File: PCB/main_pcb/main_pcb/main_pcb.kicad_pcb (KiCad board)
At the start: 2 copper layers, 163.5 x 133.5 mm, 55 parts, among them J1 Conn_01x20_Socket, J2 Conn_01x20_Socket, J3 Conn_01x09_Socket, SW0_Header1 B6B-XH-A, SW1_Header1 B6B-XH-A

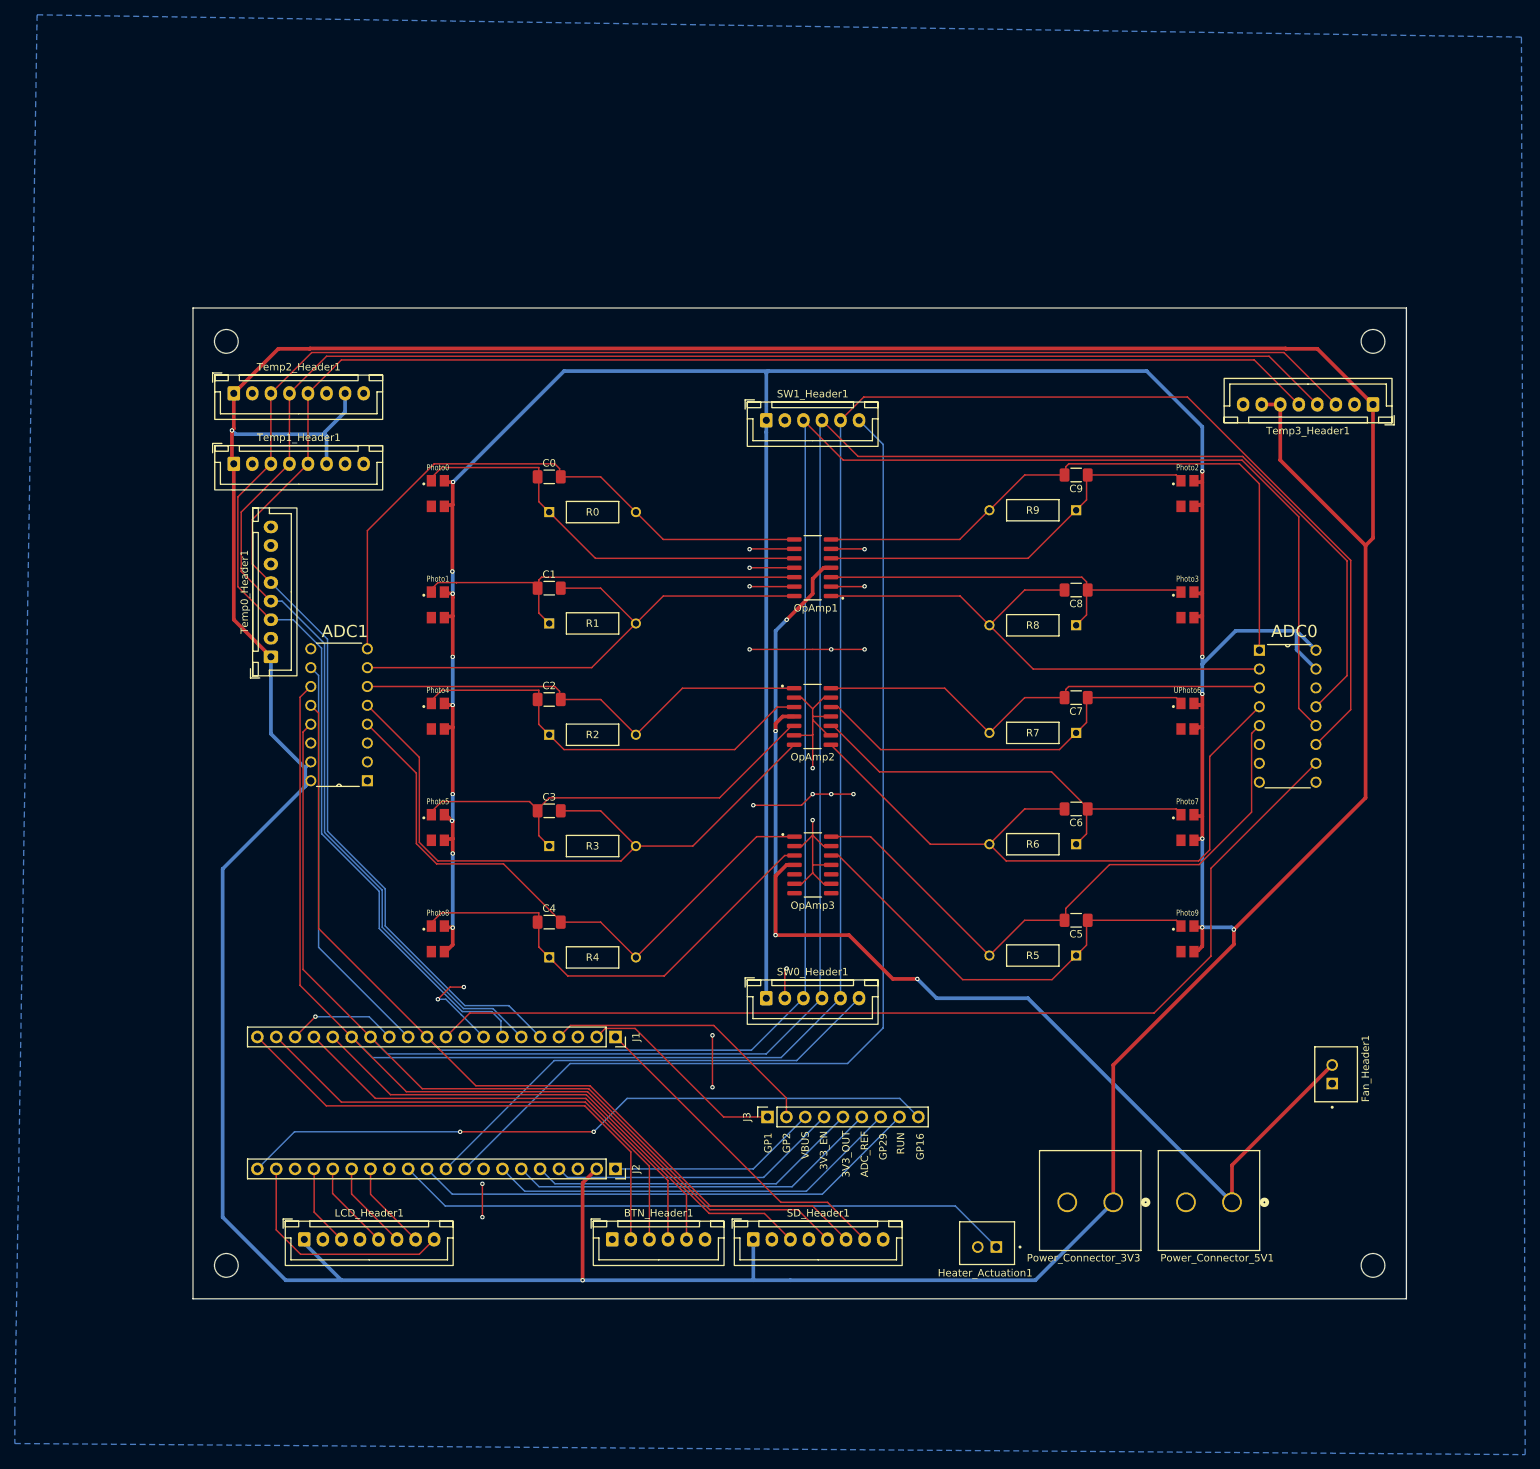
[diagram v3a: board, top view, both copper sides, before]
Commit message: Fully seperated analog ground from digital ground on the main PCB.
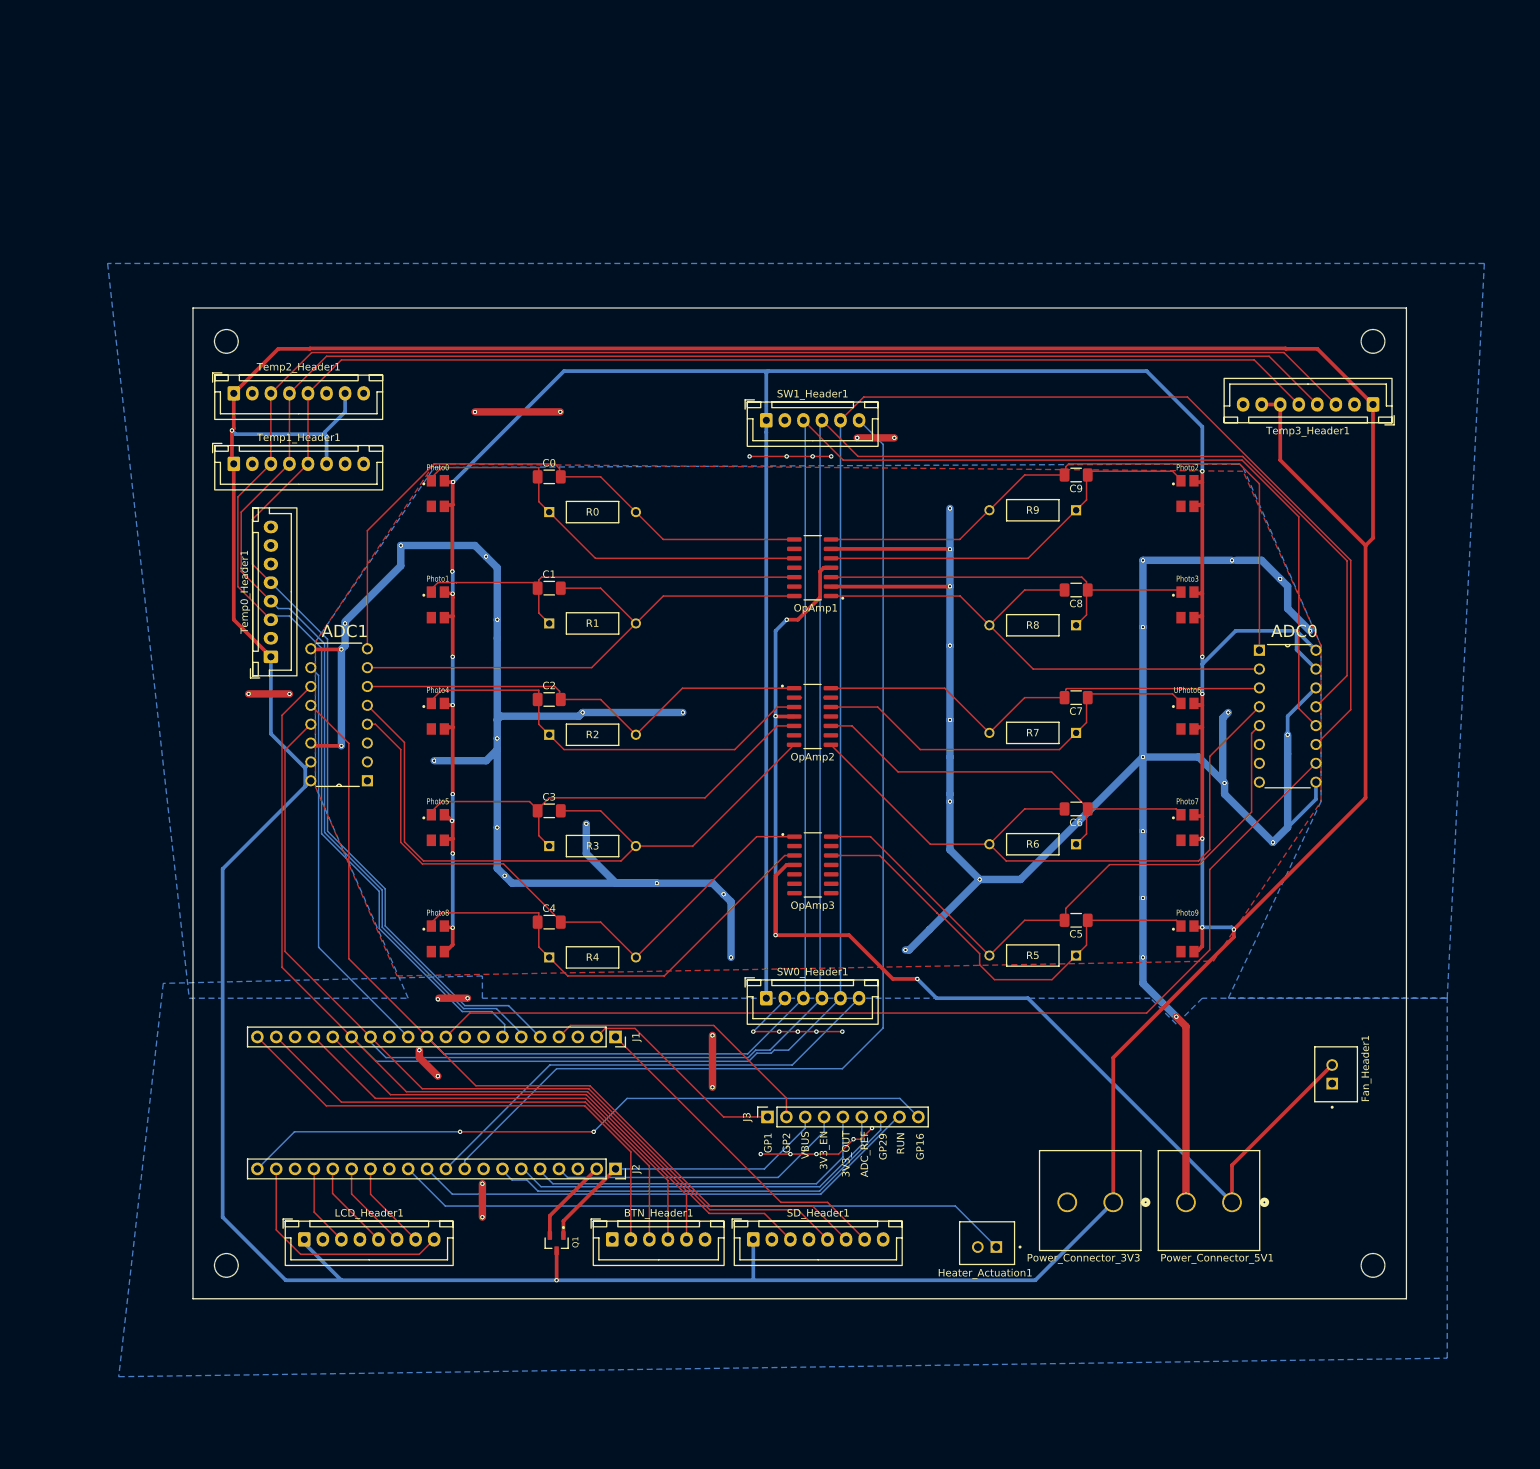
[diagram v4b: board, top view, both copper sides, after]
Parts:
- added Q1: DMG2305UX-7, DMG2305UX_7:SOT91P240X110-3N_DMG2305UX-7, F.Cu at (66.5, 163.5)
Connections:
- J2 pad 2: +3.3V -> VSYS
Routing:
- net GND: track 144.3 -> 581.7 mm, vias 22 -> 66
- net VBUS: track 28.5 -> 41.2 mm
- net +3.3V: track 994.7 -> 982.8 mm
- net VSYS: track 0.00 -> 11.6 mm
- net 3V3_OUT: track 45.4 -> 48.7 mm
- net SPI1_SCK: track 362.2 -> 365.0 mm
- net SPI1_MOSI: track 375.2 -> 377.7 mm
- net ADC_VREF: track 50.8 -> 53.0 mm
- net OpOut8: track 83.0 -> 84.8 mm
- net GPIO29: track 56.3 -> 57.5 mm
- net 3V3_EN: track 39.6 -> 40.7 mm
- net OpOut5: track 91.6 -> 92.8 mm
- net OpIn9: track 60.0 -> 60.9 mm
- net I2C0_SCL: track 256.2 -> 256.9 mm
- net OpIn2: track 54.5 -> 55.2 mm
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- added copper zone on F.Cu, net GND

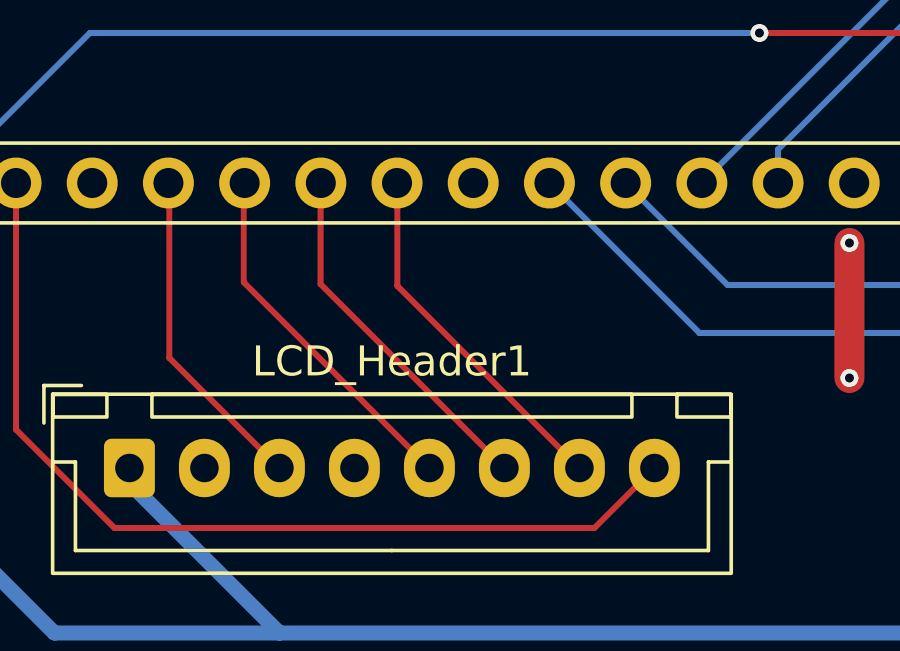
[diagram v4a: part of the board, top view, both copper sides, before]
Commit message: Switched around regsel and reset pins for display header on main PCB.
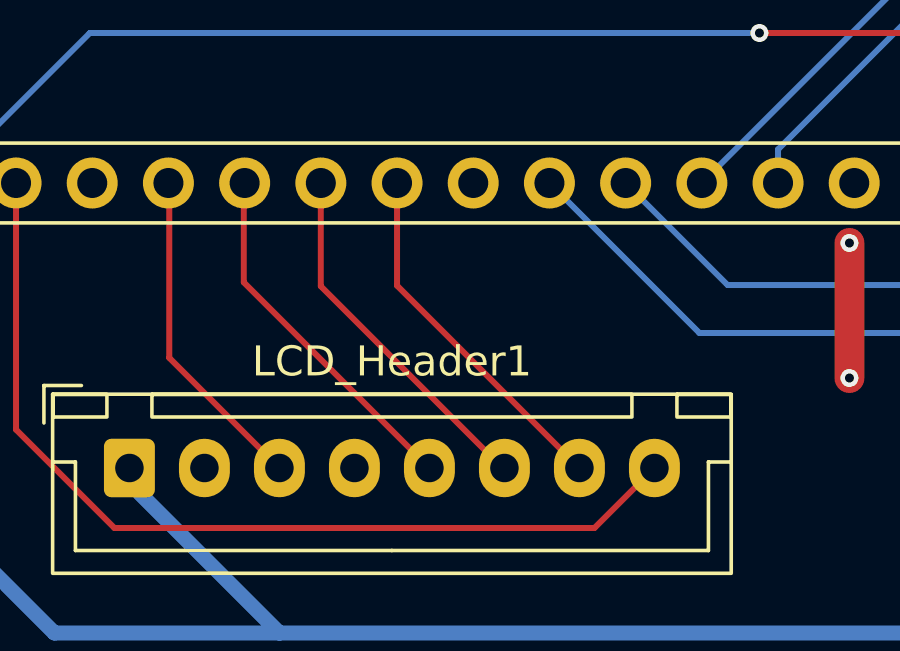
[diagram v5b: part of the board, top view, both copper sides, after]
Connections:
- J2 pad 14: DISP_RST -> DISP REGSEL
- J2 pad 15: DISP REGSEL -> DISP_RST
- LCD_Header1 pad 6: DISP REGSEL -> DISP_RST
- LCD_Header1 pad 7: DISP_RST -> DISP REGSEL
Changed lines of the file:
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@@
 			(layers "*.Cu" "*.Mask")
 			(remove_unused_layers no)
-			(net 47 "DISP_RST")
+			(net 43 "DISP REGSEL")
 			(pinfunction "Pin_14")
 			(pintype "passive")
@@
 			(layers "*.Cu" "*.Mask")
 			(remove_unused_layers no)
-			(net 43 "DISP REGSEL")
+			(net 47 "DISP_RST")
 			(pinfunction "Pin_15")
 			(pintype "passive")
@@
 			(layer "F.Fab")
 		)
+		(fp_text user "${REFERENCE}"
+			(at -2 7.5 0)
+			(unlocked yes)
+			(layer "F.Fab")
+			(effects
+				(font
+					(size 1 1)
+					(thickness 0.15)
+				)
+			)
+		)
 		(pad "1" thru_hole circle
 			(at 0 0)
@@
 			(layers "*.Cu" "*.Mask")
 			(remove_unused_layers no)
-			(net 43 "DISP REGSEL")
+			(net 47 "DISP_RST")
 			(pinfunction "6")
 			(pintype "passive")
@@
 			(layers "*.Cu" "*.Mask")
 			(remove_unused_layers no)
-			(net 47 "DISP_RST")
+			(net 43 "DISP REGSEL")
 			(pinfunction "7")
 			(pintype "passive")
@@
 			(layer "F.Fab")
 		)
+		(fp_text user "${REFERENCE}"
+			(at -4 7.5 0)
+			(unlocked yes)
+			(layer "F.Fab")
+			(effects
+				(font
+					(size 1 1)
+					(thickness 0.15)
+				)
+			)
+		)
 		(pad "1" thru_hole circle
 			(at 0 0)
@@
 	)
 	(segment
-		(start 38.871067 156.871067)
-		(end 38.871067 153.508933)
+		(start 41.42 153.5)
+		(end 41.42 156.92)
 		(width 0.2)
 		(layer "F.Cu")
@@
 	)
 	(segment
-		(start 45 163)
-		(end 38.871067 156.871067)
+		(start 41.42 156.92)
+		(end 47.5 163)
 		(width 0.2)
 		(layer "F.Cu")
@@
 	)
 	(segment
-		(start 38.871067 153.508933)
-		(end 38.88 153.5)
+		(start 41.429981 153.509981)
+		(end 41.42 153.5)
 		(width 0.2)
 		(layer "F.Cu")
@@
 	)
 	(segment
-		(start 47.5 163)
-		(end 41.429981 156.929981)
+		(start 44.94 163)
+		(end 38.88 156.94)
 		(width 0.2)
 		(layer "F.Cu")
@@
 	)
 	(segment
-		(start 41.429981 153.509981)
-		(end 41.42 153.5)
+		(start 38.88 156.94)
+		(end 38.88 153.5)
 		(width 0.2)
 		(layer "F.Cu")
@@
 	)
 	(segment
-		(start 41.429981 156.929981)
-		(end 41.429981 153.509981)
+		(start 45 163)
+		(end 44.94 163)
+		(width 0.2)
+		(layer "F.Cu")
+		(net 47)
+	)
+	(segment
+		(start 38.871067 153.508933)
+		(end 38.88 153.5)
 		(width 0.2)
 		(layer "F.Cu")
@@
 	)
 	(segment
-		(start 33.828501 153.528501)
-		(end 33.8 153.5)
+		(start 37.5 163)
+		(end 33.828501 159.328501)
 		(width 0.2)
 		(layer "F.Cu")
@@
 	)
 	(segment
-		(start 37.5 163)
-		(end 33.828501 159.328501)
+		(start 33.828501 153.528501)
+		(end 33.8 153.5)
 		(width 0.2)
 		(layer "F.Cu")
@@
 			(pts
 				(xy 158.5 58.5) (xy 159 59) (xy 169.5 83) (xy 169.5 104) (xy 157 130.5) (xy 186.5 130.5) (xy 191.5 31.5)
-				(xy 6 31.5) (xy 17 130.5) (xy 46.5 130.5) (xy 34 102) (xy 34 82.5) (xy 50 59) (xy 158 58.5) (xy 158 58.5)
+				(xy 6 31.5) (xy 17 130.5) (xy 46.5 130.5) (xy 34 102) (xy 34 82.5) (xy 50 59) (xy 158 58.5)
 			)
 		)

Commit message: A lot of changes, display logic and some error handling
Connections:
- net DISP REGSEL renamed DISP RST
- net DISP_RST renamed DISP_A0
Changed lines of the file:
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@@
 	(net 41 "ADC_VREF")
 	(net 42 "3V3_OUT")
-	(net 43 "DISP REGSEL")
+	(net 43 "DISP RST")
 	(net 44 "+3.3V")
 	(net 45 "HEATER_ON")
 	(net 46 "SPI1_CSn_TD1")
-	(net 47 "DISP_RST")
+	(net 47 "DISP_A0")
 	(net 48 "SPI1_MOSI")
 	(net 49 "SPI0_SCK")
@@
 			(layers "*.Cu" "*.Mask")
 			(remove_unused_layers no)
-			(net 43 "DISP REGSEL")
+			(net 43 "DISP RST")
 			(pinfunction "Pin_14")
 			(pintype "passive")
@@
 			(layers "*.Cu" "*.Mask")
 			(remove_unused_layers no)
-			(net 47 "DISP_RST")
+			(net 47 "DISP_A0")
 			(pinfunction "Pin_15")
 			(pintype "passive")
@@
 			(layers "*.Cu" "*.Mask")
 			(remove_unused_layers no)
-			(net 47 "DISP_RST")
+			(net 47 "DISP_A0")
 			(pinfunction "6")
 			(pintype "passive")
@@
 			(layers "*.Cu" "*.Mask")
 			(remove_unused_layers no)
-			(net 43 "DISP REGSEL")
+			(net 43 "DISP RST")
 			(pinfunction "7")
 			(pintype "passive")
